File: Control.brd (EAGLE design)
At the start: 93.7 x 34.3 mm, 20 parts, among them IC1 MEGA8-P, Q1 16MHz, T1 2N2222, X1 MKDSN1,5/3-5,08, X2 MKDSN1,5/3-5,08

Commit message: updated schematic and board
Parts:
- added R7: 120K, rcl:0207/7
- moved R6 8.89 mm to (78.7, 3.81)
- moved R1 1.27 mm to (16.5, 3.81)
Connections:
- net GND: now also R7.2
- net N$18: now also R7.1
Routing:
- net N$5: track 14.6 -> 5.72 mm
- net N$22: track 9.20 -> 4.34 mm
- net N$18: track 46.0 -> 49.8 mm
- net N$19: track 27.3 -> 26.2 mm
- net N$1: track 20.6 -> 21.6 mm
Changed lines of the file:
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@@
 <layer number="25" name="tNames" color="7" fill="1" visible="yes" active="yes"/>
 <layer number="26" name="bNames" color="7" fill="1" visible="yes" active="yes"/>
-<layer number="27" name="tValues" color="7" fill="1" visible="no" active="yes"/>
+<layer number="27" name="tValues" color="7" fill="1" visible="yes" active="yes"/>
 <layer number="28" name="bValues" color="7" fill="1" visible="no" active="yes"/>
 <layer number="29" name="tStop" color="7" fill="3" visible="no" active="yes"/>
@@
 </autorouter>
 <elements>
-<element name="R1" library="rcl" package="0414/15" value="5M" x="17.78" y="3.81" smashed="yes" rot="R180">
-<attribute name="NAME" x="16.256" y="5.0546" size="1.27" layer="25" ratio="10" rot="R180"/>
-<attribute name="VALUE" x="22.098" y="4.3942" size="1.27" layer="25" ratio="10" rot="R180"/>
+<element name="R1" library="rcl" package="0414/15" value="5M" x="16.51" y="3.81" smashed="yes" rot="R180">
+<attribute name="NAME" x="14.986" y="5.0546" size="1.27" layer="25" ratio="10" rot="R180"/>
+<attribute name="VALUE" x="20.828" y="4.3942" size="1.27" layer="25" ratio="10" rot="R180"/>
 </element>
 <element name="R2" library="rcl" package="0414/15" value="1.1M" x="24.13" y="24.13" smashed="yes" rot="R270">
@@
 <attribute name="VALUE" x="49.53" y="27.559" size="1.27" layer="25" ratio="10" rot="R270"/>
 </element>
-<element name="R6" library="rcl" package="0411/12" value="220" x="87.63" y="3.81" smashed="yes">
-<attribute name="NAME" x="85.09" y="3.683" size="1.27" layer="25" ratio="10"/>
-<attribute name="VALUE" x="89.1286" y="3.175" size="1.27" layer="25" ratio="10"/>
+<element name="R6" library="rcl" package="0411/12" value="220" x="78.74" y="3.81" smashed="yes">
+<attribute name="NAME" x="76.2" y="3.683" size="1.27" layer="25" ratio="10"/>
+<attribute name="VALUE" x="80.2386" y="3.175" size="1.27" layer="25" ratio="10"/>
 </element>
 <element name="Q1" library="crystal" package="TC38H" value="16MHz" x="74.93" y="16.51" smashed="yes">
@@
 </element>
 <element name="C4" library="rcl" package="C025-024X044" value="" x="80.01" y="11.43"/>
+<element name="R7" library="rcl" package="0207/7" value="120K" x="24.13" y="10.16" rot="R90"/>
 </elements>
 <signals>
@@
 <wire x1="13.9489" y1="22.885" x2="13.9489" y2="13.995" width="1.6764" layer="1"/>
 <wire x1="13.9489" y1="13.995" x2="13.9489" y2="7.5989" width="1.016" layer="1"/>
-<wire x1="13.9489" y1="7.5989" x2="10.16" y2="3.81" width="1.016" layer="1" curve="-90"/>
+<wire x1="13.9489" y1="7.5989" x2="8.89" y2="3.81" width="1.016" layer="1" curve="-90"/>
 </signal>
 <signal name="GND">
@@
 <wire x1="81.28" y1="7.62" x2="81.28" y2="11.43" width="0.6096" layer="1"/>
 <polygon width="1.016" layer="16" isolate="0.6096">
-<vertex x="17.78" y="25.4"/>
-<vertex x="17.78" y="11.43"/>
+<vertex x="19.05" y="25.4"/>
+<vertex x="17.78" y="6.35"/>
 <vertex x="24.13" y="0"/>
 <vertex x="74.93" y="1.27"/>
@@
 <wire x1="62.23" y1="3.81" x2="62.23" y2="11.43" width="0.8128" layer="16"/>
 <wire x1="62.23" y1="11.43" x2="59.69" y2="13.97" width="0.8128" layer="16" curve="90"/>
+<contactref element="R7" pad="2"/>
 </signal>
 <signal name="N$4">
@@
 <wire x1="62.23" y1="16.51" x2="63.5" y2="15.24" width="0.6096" layer="16"/>
 <contactref element="R1" pad="1"/>
-<wire x1="29.21" y1="3.81" x2="25.4" y2="3.81" width="0.6096" layer="16"/>
+<wire x1="29.21" y1="3.81" x2="24.13" y2="3.81" width="0.6096" layer="16"/>
+<contactref element="R7" pad="1"/>
+<wire x1="24.13" y1="3.81" x2="24.13" y2="6.35" width="0.8128" layer="16"/>
 </signal>
 <signal name="N$19">
@@
 <wire x1="57.277" y1="16.637" x2="60.96" y2="19.05" width="0.6096" layer="1"/>
 <wire x1="57.15" y1="13.97" x2="57.15" y2="16.637" width="0.6096" layer="1"/>
-<wire x1="57.15" y1="13.97" x2="55.88" y2="10.16" width="0.6096" layer="1"/>
-<wire x1="55.88" y1="10.16" x2="60.96" y2="5.08" width="0.6096" layer="1"/>
+<wire x1="57.15" y1="13.97" x2="57.15" y2="10.16" width="0.6096" layer="1"/>
+<wire x1="57.15" y1="10.16" x2="60.96" y2="5.08" width="0.6096" layer="1"/>
 <wire x1="60.96" y1="5.08" x2="64.77" y2="5.08" width="0.6096" layer="1"/>
 </signal>
@@
 <contactref element="IC1" pad="24"/>
 <contactref element="R6" pad="2"/>
-<wire x1="86.36" y1="7.62" x2="90.17" y2="3.81" width="0.4064" layer="1" curve="90"/>
-<wire x1="90.17" y1="3.81" x2="93.98" y2="3.81" width="0.4064" layer="1"/>
+<wire x1="86.36" y1="7.62" x2="86.36" y2="5.08" width="0.8128" layer="1"/>
+<wire x1="86.36" y1="5.08" x2="85.09" y2="3.81" width="0.8128" layer="1" curve="-90"/>
 </signal>
 <signal name="N$5">
 <contactref element="T1" pad="2"/>
 <contactref element="R6" pad="1"/>
-<wire x1="66.675" y1="3.81" x2="81.28" y2="3.81" width="0.6096" layer="1"/>
+<wire x1="66.675" y1="3.81" x2="72.39" y2="3.81" width="0.6096" layer="1"/>
 </signal>
 <signal name="N$20">

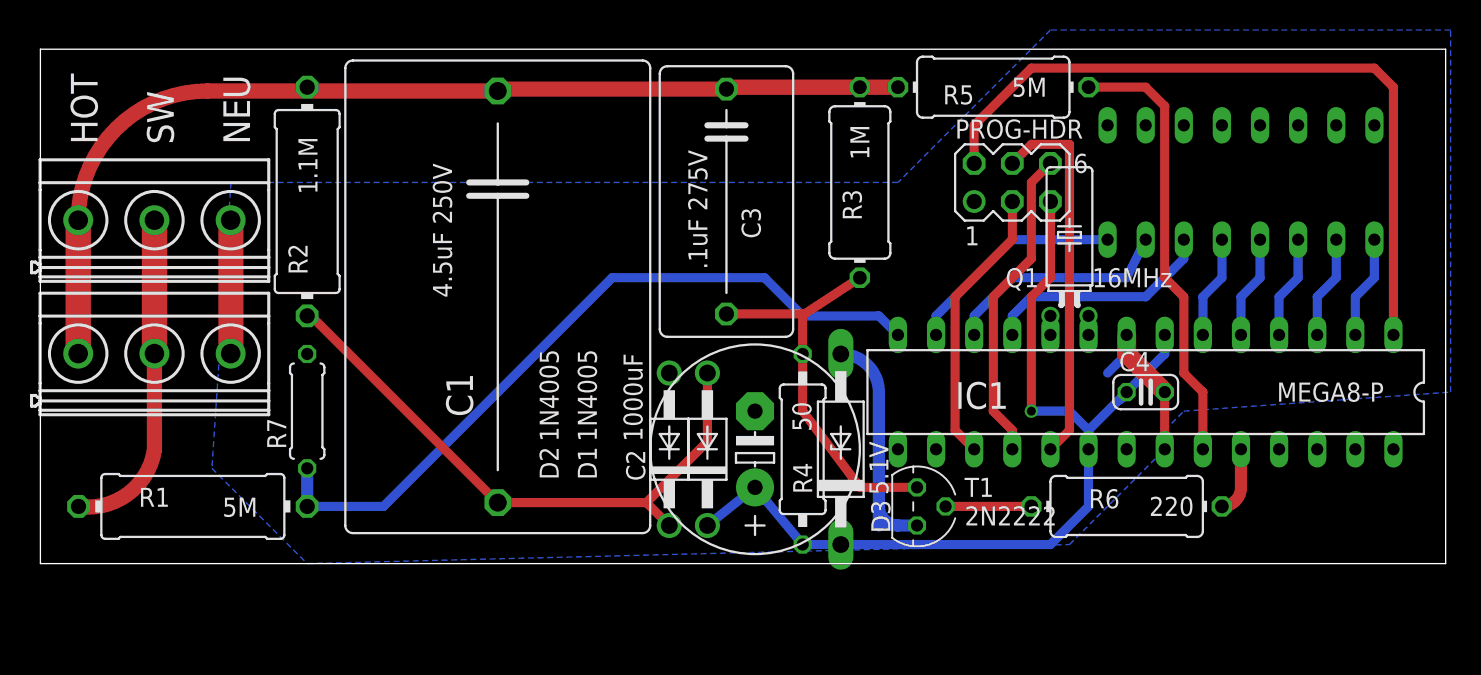
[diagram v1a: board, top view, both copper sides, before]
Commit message: Updated schematic and board to add needed pullup resistor to reset pin on Atmega. Also added surface mount pads for local filter capacitor. Pullup resistor located to fit inside central channel of a DIP socket. Changes needed discovered at first hardware assembly.
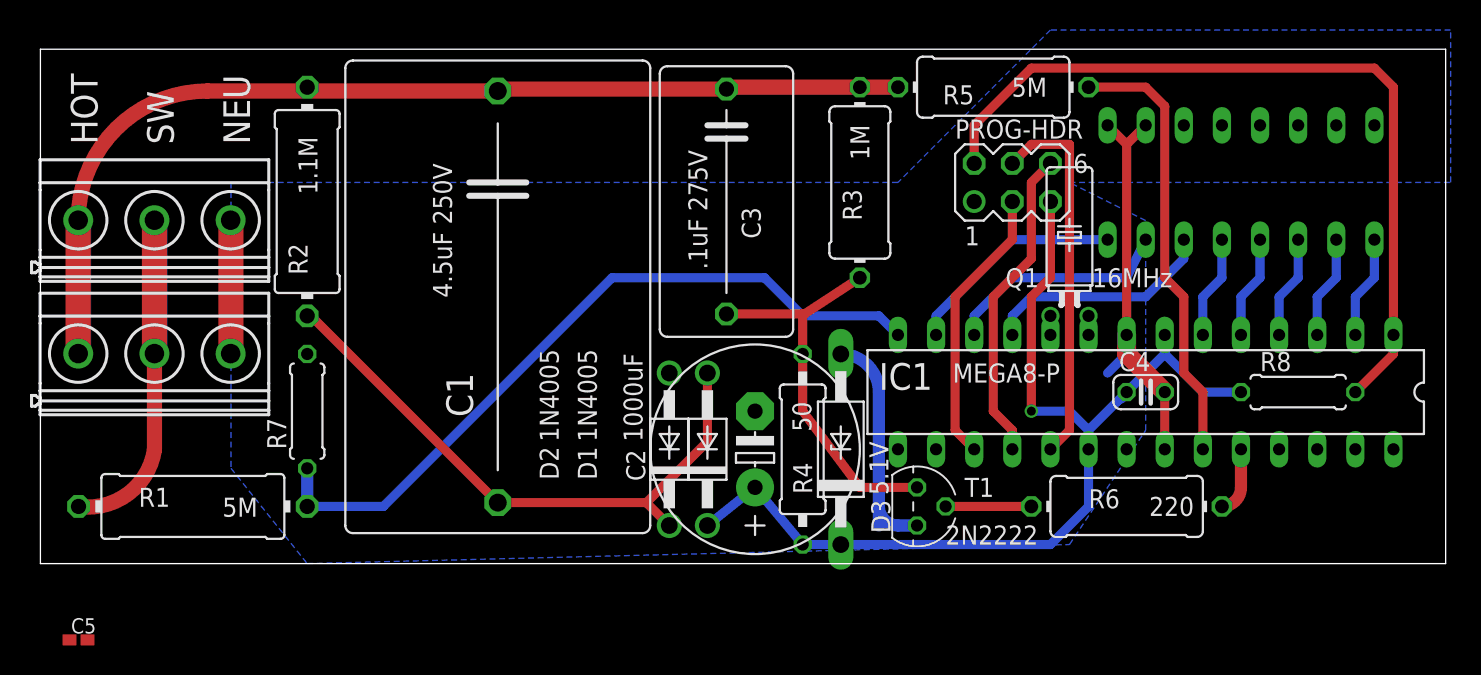
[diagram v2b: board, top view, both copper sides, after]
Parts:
- added C5: (no value), rcl:C0402K
- added R8: 120K, rcl:0207/7
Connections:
- net +5V: now also C5.1, R8.1
- net GND: now also C5.2
- net N$8: now also R8.2
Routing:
- net GND: track 27.3 -> 43.6 mm
- net +5V: track 62.4 -> 68.5 mm
- net N$8: track 49.1 -> 54.0 mm
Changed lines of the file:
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@@
 <attribute name="MF" value="" x="80.01" y="11.43" size="1.778" layer="27" rot="R180" display="off"/>
 <attribute name="OC_NEWARK" value="unknown" x="80.01" y="11.43" size="1.778" layer="27" rot="R180" display="off"/>
-<attribute name="NAME" x="67.31" y="10.3124" size="1.778" layer="25" ratio="10"/>
-<attribute name="VALUE" x="95.885" y="12.065" size="1.27" layer="25" ratio="10" rot="R180"/>
+<attribute name="NAME" x="62.23" y="11.5824" size="1.778" layer="25" ratio="10"/>
+<attribute name="VALUE" x="74.295" y="13.335" size="1.27" layer="25" ratio="10" rot="R180"/>
 </element>
 <element name="PROG-HDR" library="con-lstb" package="MA03-2" value="" x="71.12" y="25.4" smashed="yes">
@@
 <element name="T1" library="transistor-neu-to92" package="TO92" value="2N2222" x="64.77" y="3.81" smashed="yes" rot="R270">
 <attribute name="NAME" x="67.945" y="4.445" size="1.27" layer="25" ratio="10"/>
-<attribute name="VALUE" x="67.945" y="2.54" size="1.27" layer="25" ratio="10"/>
+<attribute name="VALUE" x="66.675" y="1.27" size="1.27" layer="25" ratio="10"/>
 </element>
 <element name="R3" library="rcl" package="0411/12" value="1M" x="60.96" y="25.4" smashed="yes" rot="R90">
@@
 <element name="C4" library="rcl" package="C025-024X044" value="" x="80.01" y="11.43"/>
 <element name="R7" library="rcl" package="0207/7" value="120K" x="24.13" y="10.16" rot="R90"/>
+<element name="R8" library="rcl" package="0207/7" value="120K" x="90.17" y="11.43" smashed="yes">
+<attribute name="NAME" x="87.63" y="12.827" size="1.27" layer="25" ratio="10"/>
+<attribute name="VALUE" x="87.884" y="10.8712" size="1.27" layer="27" ratio="10"/>
+</element>
+<element name="C5" library="rcl" package="C0402K" value="" x="8.89" y="-5.08"/>
 </elements>
 <signals>
@@
 <polygon width="1.016" layer="16" isolate="0.6096">
 <vertex x="19.05" y="25.4"/>
-<vertex x="17.78" y="6.35"/>
+<vertex x="19.05" y="6.35"/>
 <vertex x="24.13" y="0"/>
 <vertex x="74.93" y="1.27"/>
-<vertex x="81.28" y="7.62"/>
-<vertex x="81.28" y="8.89"/>
-<vertex x="82.55" y="10.16"/>
-<vertex x="100.33" y="11.43"/>
+<vertex x="80.01" y="8.89"/>
+<vertex x="80.01" y="22.86"/>
+<vertex x="74.93" y="25.4"/>
+<vertex x="100.33" y="25.4"/>
 <vertex x="100.33" y="35.56"/>
 <vertex x="73.66" y="35.56"/>
@@
 <wire x1="62.23" y1="11.43" x2="59.69" y2="13.97" width="0.8128" layer="16" curve="90"/>
 <contactref element="R7" pad="2"/>
+<wire x1="78.74" y1="15.24" x2="78.74" y2="27.94" width="0.6096" layer="1"/>
+<wire x1="78.74" y1="27.94" x2="77.47" y2="29.21" width="0.6096" layer="1"/>
+<wire x1="78.74" y1="27.94" x2="80.01" y2="29.21" width="0.6096" layer="1"/>
+<contactref element="C5" pad="2"/>
+<wire x1="19.0289" y1="13.995" x2="9.49" y2="-5.08" width="0" layer="19" extent="1-1"/>
 </signal>
 <signal name="N$4">
@@
 <wire x1="72.39" y1="33.02" x2="68.58" y2="29.21" width="0.6096" layer="1"/>
 <wire x1="68.58" y1="29.21" x2="68.58" y2="26.67" width="0.6096" layer="1"/>
+<contactref element="R8" pad="2"/>
+<wire x1="93.98" y1="11.43" x2="96.52" y2="13.97" width="0.6096" layer="1"/>
+<wire x1="96.52" y1="13.97" x2="96.52" y2="15.24" width="0.6096" layer="1"/>
 </signal>
 <signal name="+5V">
@@
 <wire x1="57.15" y1="1.27" x2="53.975" y2="5.08" width="0.6096" layer="16"/>
 <wire x1="78.74" y1="11.43" x2="78.105" y2="10.795" width="0.4064" layer="16" curve="-90"/>
+<contactref element="R8" pad="1"/>
+<wire x1="86.36" y1="11.43" x2="83.82" y2="11.43" width="0.6096" layer="16"/>
+<wire x1="83.82" y1="11.43" x2="81.28" y2="13.97" width="0.6096" layer="16"/>
+<contactref element="C5" pad="1"/>
+<wire x1="8.29" y1="-5.08" x2="50.8" y2="2.54" width="0" layer="19" extent="1-1"/>
 </signal>
 <signal name="N$9">

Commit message: last updated board
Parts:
- moved C5 73.0 mm to (80.0, 11.4)
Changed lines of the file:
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@@
 <attribute name="VALUE" x="87.884" y="10.8712" size="1.27" layer="27" ratio="10"/>
 </element>
-<element name="C5" library="rcl" package="C0402K" value="" x="8.89" y="-5.08"/>
+<element name="C5" library="rcl" package="C0402K" value="" x="80.01" y="11.43"/>
 </elements>
 <signals>
@@
 <vertex x="80.01" y="8.89"/>
 <vertex x="80.01" y="22.86"/>
-<vertex x="74.93" y="25.4"/>
-<vertex x="100.33" y="25.4"/>
-<vertex x="100.33" y="35.56"/>
-<vertex x="73.66" y="35.56"/>
+<vertex x="69.85" y="27.94"/>
+<vertex x="96.52" y="29.21"/>
+<vertex x="67.31" y="29.21"/>
 <vertex x="63.5" y="25.4"/>
 </polygon>
@@
 <wire x1="78.74" y1="27.94" x2="80.01" y2="29.21" width="0.6096" layer="1"/>
 <contactref element="C5" pad="2"/>
-<wire x1="19.0289" y1="13.995" x2="9.49" y2="-5.08" width="0" layer="19" extent="1-1"/>
+<wire x1="81.28" y1="11.43" x2="80.61" y2="11.43" width="0" layer="19" extent="1-1"/>
 </signal>
 <signal name="N$4">
@@
 <wire x1="83.82" y1="11.43" x2="81.28" y2="13.97" width="0.6096" layer="16"/>
 <contactref element="C5" pad="1"/>
-<wire x1="8.29" y1="-5.08" x2="50.8" y2="2.54" width="0" layer="19" extent="1-1"/>
+<wire x1="78.74" y1="11.43" x2="79.41" y2="11.43" width="0" layer="19" extent="1-16"/>
 </signal>
 <signal name="N$9">
